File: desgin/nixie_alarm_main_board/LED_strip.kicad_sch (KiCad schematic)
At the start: 1 part, among them J2 JST XH 2.54 3 pin

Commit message: filter caps
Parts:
- added C24: 100nF 25V, GRM033D70J224ME01D, symbol SamacSys_Parts:GRM033R71E101KA01J
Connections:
- net +5V: now also C24.1
- net GND: now also C24.2
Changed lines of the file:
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@@
 	(generator_version "8.0")
 	(paper "A4")
+	(junction
+		(at 158.75 92.202)
+		(diameter 0)
+		(color 0 0 0 0)
+	)
 	(wire
 		(pts
-			(xy 145.542 94.742) (xy 153.162 94.742)
+			(xy 145.542 94.742) (xy 165.608 94.742)
 		)
 		(stroke
@@
 	(wire
 		(pts
-			(xy 145.542 92.202) (xy 153.162 92.202)
+			(xy 158.75 92.202) (xy 165.608 92.202)
 		)
 		(stroke
@@
 		)
 	)
+	(wire
+		(pts
+			(xy 158.75 85.852) (xy 158.75 92.202)
+		)
+		(stroke
+			(width 0)
+			(type default)
+		)
+	)
+	(wire
+		(pts
+			(xy 145.542 92.202) (xy 158.75 92.202)
+		)
+		(stroke
+			(width 0)
+			(type default)
+		)
+	)
 	(global_label "+5V"
 		(shape input)
-		(at 153.162 92.202 0)
+		(at 165.608 92.202 0)
 		(fields_autoplaced yes)
 		(effects
@@
 		)
 		(property "Intersheetrefs" "${INTERSHEET_REFS}"
-			(at 160.0177 92.202 0)
+			(at 172.4637 92.202 0)
 			(effects
 				(font
@@
 	(hierarchical_label "LED_DATA"
 		(shape input)
-		(at 153.162 94.742 0)
+		(at 165.608 94.742 0)
 		(fields_autoplaced yes)
 		(effects
@@
 	)
 	(symbol
+		(lib_id "SamacSys_Parts:GRM033R71E101KA01J")
+		(at 158.75 85.852 90)
+		(unit 1)
+		(exclude_from_sim no)
+		(in_bom yes)
+		(on_board yes)
+		(dnp no)
+		(property "Reference" "C24"
+			(at 153.162 81.534 90)
+			(effects
+				(font
+					(size 1.27 1.27)
+				)
+				(justify right)
+			)
+		)
+		(property "Value" "100nF 25V"
+			(at 145.288 79.502 90)
+			(effects
+				(font
+					(size 1.27 1.27)
+				)
+				(justify right)
+			)
+		)
+		(property "Footprint" "GRM033D70J224ME01D"
+			(at 254.94 76.962 0)
+			(effects
+				(font
+					(size 1.27 1.27)
+				)
+				(justify left top)
+				(hide yes)
+			)
+		)
+		(property "Datasheet" "https://search.murata.co.jp/Ceramy/image/img/A01X/G101/ENG/GRM033R71E101KA01-01A.pdf"
+			(at 354.94 76.962 0)
+			(effects
+				(font
+					(size 1.27 1.27)
+				)
+				(justify left top)
+				(hide yes)
+			)
+		)
+		(property "Description" "Multilayer Ceramic Capacitors MLCC - SMD/SMT 100pF 25 volts 10%"
+			(at 158.75 85.852 0)
+			(effects
+				(font
+					(size 1.27 1.27)
+				)
+				(hide yes)
+			)
+		)
+		(property "Height" "0.5"
+			(at 554.94 76.962 0)
+			(effects
+				(font
+					(size 1.27 1.27)
+				)
+				(justify left top)
+				(hide yes)
+			)
+		)
+		(property "Mouser Part Number" "81-GRM033R71E101KA1J"
+			(at 654.94 76.962 0)
+			(effects
+				(font
+					(size 1.27 1.27)
+				)
+				(justify left top)
+				(hide yes)
+			)
+		)
+		(property "Mouser Price/Stock" "https://www.mouser.co.uk/ProductDetail/Murata-Electronics/GRM033R71E101KA01J?qs=563MOeNa05Lmru4oTW10Jw%3D%3D"
+			(at 754.94 76.962 0)
+			(effects
+				(font
+					(size 1.27 1.27)
+				)
+				(justify left top)
+				(hide yes)
+			)
+		)
+		(property "Manufacturer_Name" "Murata Electronics"
+			(at 854.94 76.962 0)
+			(effects
+				(font
+					(size 1.27 1.27)
+				)
+				(justify left top)
+				(hide yes)
+			)
+		)
+		(property "Manufacturer_Part_Number" "GRM033R71E101KA01J"
+			(at 954.94 76.962 0)
+			(effects
+				(font
+					(size 1.27 1.27)
+				)
+				(justify left top)
+				(hide yes)
+			)
+		)
+		(pin "1"
+		)
+		(pin "2"
+		)
+		(instances
+			(project "nixie_alarm_main_board"
+				(path "/a0d555d7-39a0-4a98-b831-70d97d0aa5a1/c8a550e7-ee44-4308-8024-1fb1e2d872b6"
+					(reference "C24")
+					(unit 1)
+				)
+			)
+		)
+	)
+	(symbol
 		(lib_id "Connector:Conn_01x03_Pin")
 		(at 140.462 94.742 0)
@@
 					(unit 1)
 				)
+			)
+		)
+	)
+	(symbol
+		(lib_id "power:GND")
+		(at 158.75 73.152 180)
+		(unit 1)
+		(exclude_from_sim no)
+		(in_bom yes)
+		(on_board yes)
+		(dnp no)
+		(fields_autoplaced yes)
+		(property "Reference" "#PWR054"
+			(at 158.75 66.802 0)
+			(effects
+				(font
+					(size 1.27 1.27)
+				)
+				(hide yes)
+			)
+		)
+		(property "Value" "GND"
+			(at 158.75 68.58 0)
+			(effects
+				(font
+					(size 1.27 1.27)
+				)
+			)
+		)
+		(property "Footprint" ""
+			(at 158.75 73.152 0)
+			(effects
+				(font
+					(size 1.27 1.27)
+				)
+				(hide yes)
+			)
+		)
+		(property "Datasheet" ""
+			(at 158.75 73.152 0)
+			(effects
+				(font
+					(size 1.27 1.27)
+				)
+				(hide yes)
+			)
+		)
+		(property "Description" "Power symbol creates a global label with name \"GND\" , ground"
+			(at 158.75 73.152 0)
+			(effects
+				(font
+					(size 1.27 1.27)
+				)
+				(hide yes)
+			)
+		)
+		(pin "1"
+		)
+		(instances
+			(project "nixie_alarm_main_board"
+				(path "/a0d555d7-39a0-4a98-b831-70d97d0aa5a1/c8a550e7-ee44-4308-8024-1fb1e2d872b6"
+					(reference "#PWR054")
+					(unit 1)
+				)

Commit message: new caps footprint
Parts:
- C24: footprint GRM033D70J224ME01D -> Capacitor_SMD:C_0805_2012Metric_Pad1.18x1.45mm_HandSolder
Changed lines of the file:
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@@
 			)
 		)
-		(property "Footprint" "GRM033D70J224ME01D"
+		(property "Footprint" "Capacitor_SMD:C_0805_2012Metric_Pad1.18x1.45mm_HandSolder"
 			(at 254.94 76.962 0)
 			(effects

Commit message: new board v1
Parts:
- J2: footprint Connector_JST:JST_XH_B3B-XH-A_1x03_P2.50mm_Vertical -> Connector_JST:JST_XH_S3B-XH-A-1_1x03_P2.50mm_Horizontal
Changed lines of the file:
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@@
 			)
 		)
-		(property "Footprint" "Connector_JST:JST_XH_B3B-XH-A_1x03_P2.50mm_Vertical"
+		(property "Footprint" "Connector_JST:JST_XH_S3B-XH-A-1_1x03_P2.50mm_Horizontal"
 			(at 140.462 94.742 0)
 			(effects

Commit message: add more detalis
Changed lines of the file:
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@@
 		(fields_autoplaced yes)
 		(property "Reference" "J2"
-			(at 141.097 86.614 0)
+			(at 141.097 87.63 0)
 			(effects
 				(font
@@
 		)
 		(property "Value" "JST XH 2.54 3 pin"
-			(at 141.097 89.154 0)
+			(at 141.097 90.17 0)
 			(effects
 				(font

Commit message: fixes added
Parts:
- added R6: 470Ω, Resistor_SMD:R_0805_2012Metric_Pad1.20x1.40mm_HandSolder, symbol SamacSys_Parts:ERJ-UP6D5101V
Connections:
- net LED_DATA: now also R6.2; no longer J2.2 (Pin_2)
- new net: J2.2 (Pin_2), R6.1
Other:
- moved on the sheet: C24, J2
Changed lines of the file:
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@@
 	(paper "A4")
 	(junction
-		(at 158.75 92.202)
+		(at 159.258 92.71)
 		(diameter 0)
 		(color 0 0 0 0)
@@
 	(wire
 		(pts
-			(xy 145.542 94.742) (xy 165.608 94.742)
+			(xy 168.91 95.25) (xy 181.61 95.25)
 		)
 		(stroke
@@
 	(wire
 		(pts
-			(xy 158.75 92.202) (xy 165.608 92.202)
+			(xy 159.258 86.36) (xy 159.258 92.71)
 		)
 		(stroke
@@
 	(wire
 		(pts
-			(xy 158.75 85.852) (xy 158.75 92.202)
+			(xy 146.05 95.25) (xy 151.13 95.25)
 		)
 		(stroke
@@
 	(wire
 		(pts
-			(xy 145.542 92.202) (xy 158.75 92.202)
+			(xy 146.05 92.71) (xy 159.258 92.71)
 		)
 		(stroke
@@
 		)
 	)
+	(wire
+		(pts
+			(xy 159.258 92.71) (xy 181.61 92.71)
+		)
+		(stroke
+			(width 0)
+			(type default)
+		)
+	)
 	(global_label "+5V"
 		(shape input)
-		(at 165.608 92.202 0)
+		(at 181.61 92.71 0)
 		(fields_autoplaced yes)
 		(effects
@@
 		)
 		(property "Intersheetrefs" "${INTERSHEET_REFS}"
-			(at 172.4637 92.202 0)
+			(at 188.4657 92.71 0)
 			(effects
 				(font
@@
 	(hierarchical_label "LED_DATA"
 		(shape input)
-		(at 165.608 94.742 0)
+		(at 181.61 95.25 0)
 		(fields_autoplaced yes)
 		(effects
@@
 	(symbol
 		(lib_id "power:GND")
-		(at 145.542 97.282 0)
+		(at 146.05 97.79 0)
 		(unit 1)
 		(exclude_from_sim no)
@@
 		(fields_autoplaced yes)
 		(property "Reference" "#PWR07"
-			(at 145.542 103.632 0)
+			(at 146.05 104.14 0)
 			(effects
 				(font
@@
 		)
 		(property "Value" "GND"
-			(at 145.542 102.362 0)
+			(at 146.05 102.87 0)
 			(effects
 				(font
@@
 		)
 		(property "Footprint" ""
-			(at 145.542 97.282 0)
+			(at 146.05 97.79 0)
 			(effects
 				(font
@@
 		)
 		(property "Datasheet" ""
-			(at 145.542 97.282 0)
+			(at 146.05 97.79 0)
 			(effects
 				(font
@@
 		)
 		(property "Description" "Power symbol creates a global label with name \"GND\" , ground"
-			(at 145.542 97.282 0)
+			(at 146.05 97.79 0)
 			(effects
 				(font
@@
 	(symbol
 		(lib_id "SamacSys_Parts:GRM033R71E101KA01J")
-		(at 158.75 85.852 90)
+		(at 159.258 86.36 90)
 		(unit 1)
 		(exclude_from_sim no)
@@
 		(dnp no)
 		(property "Reference" "C24"
-			(at 153.162 81.534 90)
+			(at 153.67 82.042 90)
 			(effects
 				(font
@@
 		)
 		(property "Value" "100nF 25V"
-			(at 145.288 79.502 90)
+			(at 145.796 80.01 90)
 			(effects
 				(font
@@
 		)
 		(property "Footprint" "Capacitor_SMD:C_0805_2012Metric_Pad1.18x1.45mm_HandSolder"
-			(at 254.94 76.962 0)
+			(at 255.448 77.47 0)
 			(effects
 				(font
@@
 		)
 		(property "Datasheet" "https://search.murata.co.jp/Ceramy/image/img/A01X/G101/ENG/GRM033R71E101KA01-01A.pdf"
-			(at 354.94 76.962 0)
+			(at 355.448 77.47 0)
 			(effects
 				(font
@@
 		)
 		(property "Description" "Multilayer Ceramic Capacitors MLCC - SMD/SMT 100pF 25 volts 10%"
-			(at 158.75 85.852 0)
+			(at 159.258 86.36 0)
 			(effects
 				(font
@@
 		)
 		(property "Height" "0.5"
-			(at 554.94 76.962 0)
+			(at 555.448 77.47 0)
 			(effects
 				(font
@@
 		)
 		(property "Mouser Part Number" "81-GRM033R71E101KA1J"
-			(at 654.94 76.962 0)
+			(at 655.448 77.47 0)
 			(effects
 				(font
@@
 		)
 		(property "Mouser Price/Stock" "https://www.mouser.co.uk/ProductDetail/Murata-Electronics/GRM033R71E101KA01J?qs=563MOeNa05Lmru4oTW10Jw%3D%3D"
-			(at 754.94 76.962 0)
+			(at 755.448 77.47 0)
 			(effects
 				(font
@@
 		)
 		(property "Manufacturer_Name" "Murata Electronics"
-			(at 854.94 76.962 0)
+			(at 855.448 77.47 0)
 			(effects
 				(font
@@
 		)
 		(property "Manufacturer_Part_Number" "GRM033R71E101KA01J"
-			(at 954.94 76.962 0)
+			(at 955.448 77.47 0)
 			(effects
 				(font
@@
 	(symbol
 		(lib_id "Connector:Conn_01x03_Pin")
-		(at 140.462 94.742 0)
+		(at 140.97 95.25 0)
 		(unit 1)
 		(exclude_from_sim no)
@@
 		(on_board yes)
 		(dnp no)
-		(fields_autoplaced yes)
 		(property "Reference" "J2"
-			(at 141.097 87.63 0)
+			(at 140.97 86.614 0)
 			(effects
 				(font
@@
 		)
 		(property "Value" "JST XH 2.54 3 pin"
-			(at 141.097 90.17 0)
+			(at 140.97 89.154 0)
 			(effects
 				(font
@@
 		)
 		(property "Footprint" "Connector_JST:JST_XH_S3B-XH-A-1_1x03_P2.50mm_Horizontal"
-			(at 140.462 94.742 0)
+			(at 140.97 95.25 0)
 			(effects
 				(font
@@
 		)
 		(property "Datasheet" "~"
-			(at 140.462 94.742 0)
+			(at 140.97 95.25 0)
 			(effects
 				(font
@@
 		)
 		(property "Description" "Generic connector, single row, 01x03, script generated"
-			(at 140.462 94.742 0)
+			(at 140.97 95.25 0)
 			(effects
 				(font
@@
 	(symbol
 		(lib_id "power:GND")
-		(at 158.75 73.152 180)
+		(at 159.258 73.66 180)
 		(unit 1)
 		(exclude_from_sim no)
@@
 		(fields_autoplaced yes)
 		(property "Reference" "#PWR054"
-			(at 158.75 66.802 0)
+			(at 159.258 67.31 0)
 			(effects
 				(font
@@
 		)
 		(property "Value" "GND"
-			(at 158.75 68.58 0)
+			(at 159.258 69.088 0)
 			(effects
 				(font
@@
 		)
 		(property "Footprint" ""
-			(at 158.75 73.152 0)
+			(at 159.258 73.66 0)
 			(effects
 				(font
@@
 		)
 		(property "Datasheet" ""
-			(at 158.75 73.152 0)
+			(at 159.258 73.66 0)
 			(effects
 				(font
@@
 		)
 		(property "Description" "Power symbol creates a global label with name \"GND\" , ground"
-			(at 158.75 73.152 0)
+			(at 159.258 73.66 0)
 			(effects
 				(font
@@
 					(unit 1)
 				)
+			)
+		)
+	)
+	(symbol
+		(lib_id "SamacSys_Parts:ERJ-UP6D5101V")
+		(at 151.13 95.25 0)
+		(unit 1)
+		(exclude_from_sim no)
+		(in_bom yes)
+		(on_board yes)
+		(dnp no)
+		(property "Reference" "R6"
+			(at 160.02 97.79 0)
+			(effects
+				(font
+					(size 1.27 1.27)
+				)
+			)
+		)
+		(property "Value" "470Ω"
+			(at 160.02 100.33 0)
+			(effects
+				(font
+					(size 1.27 1.27)
+				)
+			)
+		)
+		(property "Footprint" "Resistor_SMD:R_0805_2012Metric_Pad1.20x1.40mm_HandSolder"
+			(at 165.1 191.44 0)
+			(effects
+				(font
+					(size 1.27 1.27)
+				)
+				(justify left top)
+				(hide yes)
+			)
+		)
+		(property "Datasheet" "https://industrial.panasonic.com/cdbs/www-data/pdf/RDP0000/AOA0000C337.pdf"
+			(at 165.1 291.44 0)
+			(effects
+				(font
+					(size 1.27 1.27)
+				)
+				(justify left top)
+				(hide yes)
+			)
+		)
+		(property "Description" "Anti-Sulfurated Thick Film Chip Resistors/ Anti-Surge Type, Power Rating (W): 0.5, Chip Size (LxW(EIA)) (mm): 2.0 x 1.25 (EIA:0805), Resistance Values (?): 5100, Resistance Tolerance (%): 0.5, T.C.R (?102/K): ?100"
+			(at 151.13 95.25 0)
+			(effects
+				(font
+					(size 1.27 1.27)
+				)
+				(hide yes)
+			)
+		)
+		(property "Height" "0.7"
+			(at 165.1 491.44 0)
+			(effects
+				(font
+					(size 1.27 1.27)
+				)
+				(justify left top)
+				(hide yes)
+			)
+		)
+		(property "Mouser Part Number" "667-ERJ-UP6D5101V"
+			(at 165.1 591.44 0)
+			(effects
+				(font
+					(size 1.27 1.27)
+				)
+				(justify left top)
+				(hide yes)
+			)
+		)
+		(property "Mouser Price/Stock" "https://www.mouser.co.uk/ProductDetail/Panasonic/ERJ-UP6D5101V?qs=ZcfC38r4Pouz7%2FLHthUDHQ%3D%3D"
+			(at 165.1 691.44 0)
+			(effects
+				(font
+					(size 1.27 1.27)
+				)
+				(justify left top)
+				(hide yes)
+			)
+		)
+		(property "Manufacturer_Name" "Panasonic"
+			(at 165.1 791.44 0)
+			(effects
+				(font
+					(size 1.27 1.27)
+				)
+				(justify left top)
+				(hide yes)
+			)
+		)
+		(property "Manufacturer_Part_Number" "ERJ-UP6D5101V"
+			(at 165.1 891.44 0)
+			(effects
+				(font
+					(size 1.27 1.27)
+				)
+				(justify left top)
+				(hide yes)
+			)
+		)
+		(pin "1"
+		)
+		(pin "2"
+		)
+		(instances
+			(project "nixie_alarm_main_board"
+				(path "/a0d555d7-39a0-4a98-b831-70d97d0aa5a1/c8a550e7-ee44-4308-8024-1fb1e2d872b6"
+					(reference "R6")
+					(unit 1)
+				)

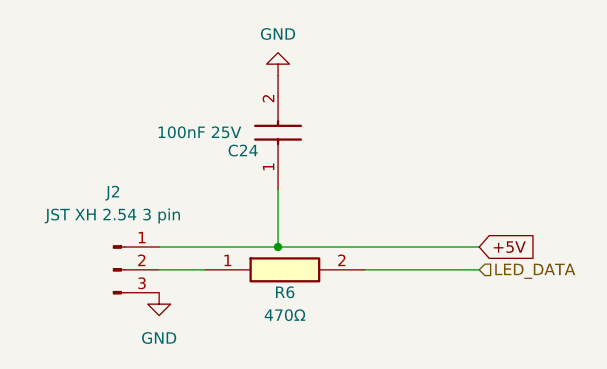
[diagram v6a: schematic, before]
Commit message: zener diode on fb
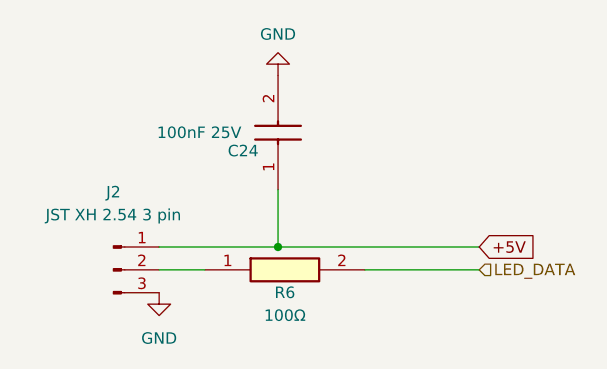
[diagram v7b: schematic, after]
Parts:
- R6: value 470Ω -> 100Ω
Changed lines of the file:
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@@
 			)
 		)
-		(property "Value" "470Ω"
+		(property "Value" "100Ω"
 			(at 160.02 100.33 0)
 			(effects
